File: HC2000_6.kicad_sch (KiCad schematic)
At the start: 31 parts, among them Q1 17,734, T2 2N2369/2N2368, T3 2N2369/BC108A

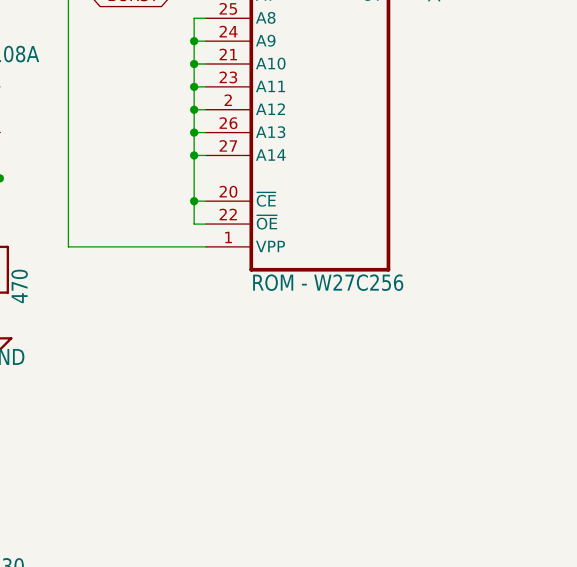
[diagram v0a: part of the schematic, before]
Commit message: Updated ICs values and positions
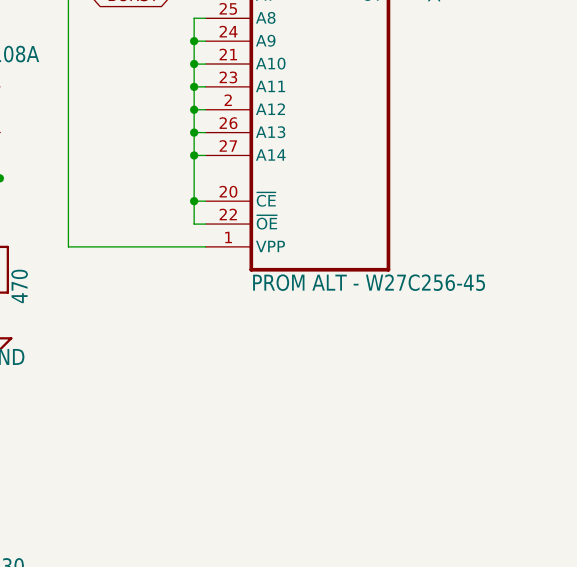
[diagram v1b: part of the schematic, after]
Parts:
- UB6: value ROM - W27C256 -> PROM ALT - W27C256-45
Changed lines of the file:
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@@
       (effects (font (size 1.778 1.5113)) (justify left bottom))
     )
-    (property "Value" "ROM - W27C256" (at 220.98 91.44 0)
+    (property "Value" "PROM ALT - W27C256-45" (at 220.98 91.44 0)
       (effects (font (size 1.778 1.5113)) (justify left bottom))
     )

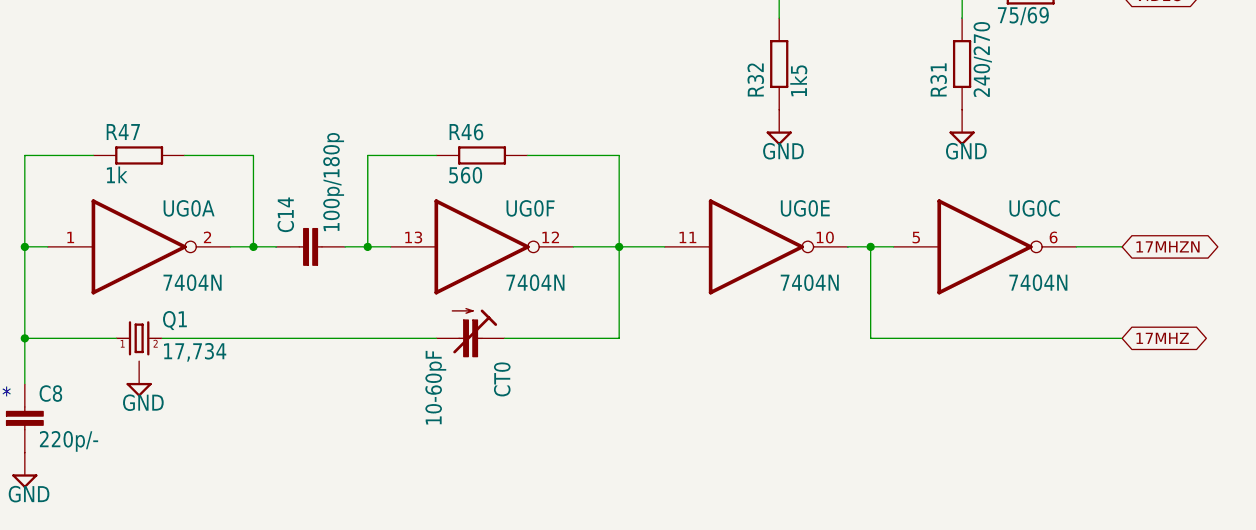
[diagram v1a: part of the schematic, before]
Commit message: Fix errors (IC & unnoticed cut for 1 EPROM)
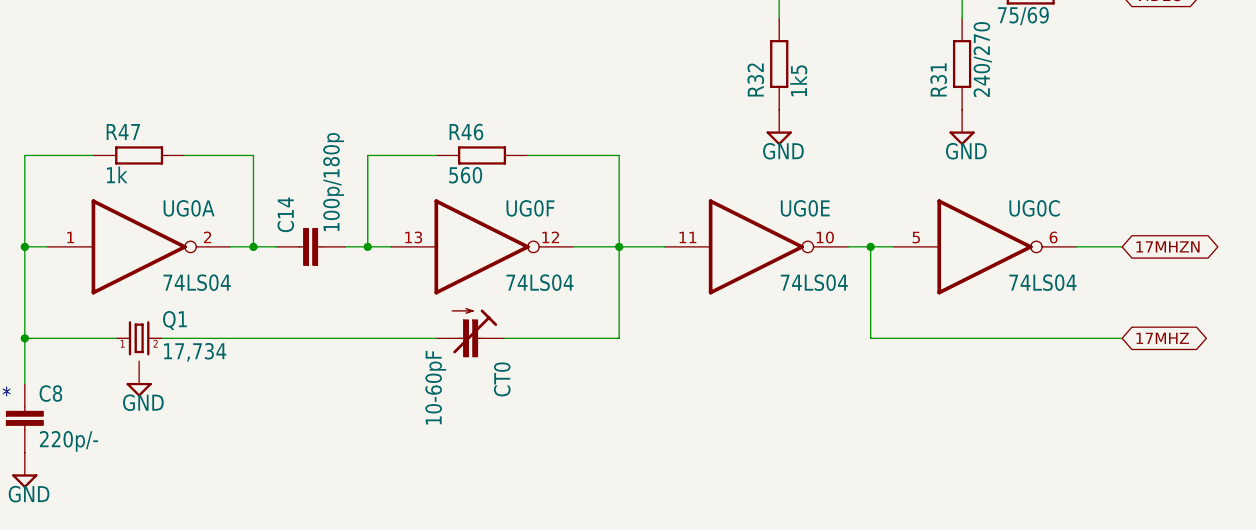
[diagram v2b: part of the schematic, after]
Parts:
- UG0: value 7404N -> 74LS04
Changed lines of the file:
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@@
       (effects (font (size 1.778 1.5113)) (justify left bottom))
     )
-    (property "Value" "7404N" (at 193.04 157.48 0)
+    (property "Value" "74LS04" (at 193.04 157.48 0)
       (effects (font (size 1.778 1.5113)) (justify left bottom))
     )
@@
       (effects (font (size 1.778 1.5113)) (justify left bottom))
     )
-    (property "Value" "7404N" (at 167.64 157.48 0)
+    (property "Value" "74LS04" (at 167.64 157.48 0)
       (effects (font (size 1.778 1.5113)) (justify left bottom))
     )
@@
       (effects (font (size 1.778 1.5113)) (justify left bottom))
     )
-    (property "Value" "7404N" (at 137.16 157.48 0)
+    (property "Value" "74LS04" (at 137.16 157.48 0)
       (effects (font (size 1.778 1.5113)) (justify left bottom))
     )
@@
       (effects (font (size 1.778 1.5113)) (justify left bottom))
     )
-    (property "Value" "7404N" (at 99.06 157.48 0)
-      (effects (font (size 1.778 1.5113)) (justify left bottom))
-    )
+    (property "Value" "74LS04" (at 99.06 157.48 0)
+      (effects (font (size 1.778 1.5113)) (justify left bottom))
+    )

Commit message: Revision-E
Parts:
- C14: value 100p/180p -> 180p
- C7: value 10p/15p -> 15p
- C8: value 220p/- -> -
- R30, R48: value 75/69 -> 69
- R31: value 240/270 -> 270
- R66: value 1k8/1k6 -> 1k6
- R68: value 5k6/5k1 -> 5k1
- T2: value 2N2369/2N2368 -> 2N2368
- T3: value 2N2369/BC108A -> BC108A
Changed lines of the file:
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@@
       (effects (font (size 1.778 1.5113)) (justify left bottom))
     )
-    (property "Value" "240/270" (at 191.262 135.89 0)
+    (property "Value" "270" (at 191.262 135.89 0)
       (effects (font (size 1.778 1.5113)) (justify left bottom))
     )
@@
       (effects (font (size 1.778 1.5113)) (justify left bottom))
     )
-    (property "Value" "100p/180p" (at 118.999 150.876 0)
+    (property "Value" "180p" (at 118.999 150.876 0)
       (effects (font (size 1.778 1.5113)) (justify left bottom))
     )
@@
       (effects (font (size 1.778 1.5113)) (justify left bottom))
     )
-    (property "Value" "2N2369/2N2368" (at 175.26 111.76 0)
+    (property "Value" "2N2368" (at 175.26 111.76 0)
       (effects (font (size 1.778 1.5113)) (justify left bottom))
     )
@@
       (effects (font (size 1.778 1.5113)) (justify left bottom))
     )
-    (property "Value" "75/69" (at 170.942 67.31 0)
+    (property "Value" "69" (at 170.942 67.31 0)
       (effects (font (size 1.778 1.5113)) (justify left bottom))
     )
@@
       (effects (font (size 1.778 1.5113)) (justify left bottom))
     )
-    (property "Value" "75/69" (at 191.77 127.762 0)
+    (property "Value" "69" (at 191.77 127.762 0)
       (effects (font (size 1.778 1.5113)) (justify left bottom))
     )
@@
       (effects (font (size 1.778 1.5113)) (justify left bottom))
     )
-    (property "Value" "2N2369/BC108A" (at 180.34 66.04 0)
+    (property "Value" "BC108A" (at 180.34 66.04 0)
       (effects (font (size 1.778 1.5113)) (justify left bottom))
     )
@@
       (effects (font (size 1.778 1.5113)) (justify left bottom))
     )
-    (property "Value" "5k6/5k1" (at 140.97 104.902 0)
+    (property "Value" "5k1" (at 140.97 104.902 0)
       (effects (font (size 1.778 1.5113)) (justify left bottom))
     )
@@
       (effects (font (size 1.778 1.5113)) (justify left bottom))
     )
-    (property "Value" "1k8/1k6" (at 140.97 120.142 0)
+    (property "Value" "1k6" (at 140.97 120.142 0)
       (effects (font (size 1.778 1.5113)) (justify left bottom))
     )
@@
       (effects (font (size 1.778 1.5113)) (justify left bottom))
     )
-    (property "Value" "220p/-" (at 85.344 174.879 0)
+    (property "Value" "-" (at 85.344 174.879 0)
       (effects (font (size 1.778 1.5113)) (justify left bottom))
     )
@@
       (effects (font (size 1.778 1.5113)) (justify left bottom))
     )
-    (property "Value" "10p/15p" (at 169.164 108.839 0)
-      (effects (font (size 1.778 1.5113)) (justify left bottom))
-    )
+    (property "Value" "15p" (at 169.164 108.839 0)
+      (effects (font (size 1.778 1.5113)) (justify left bottom))
+    )

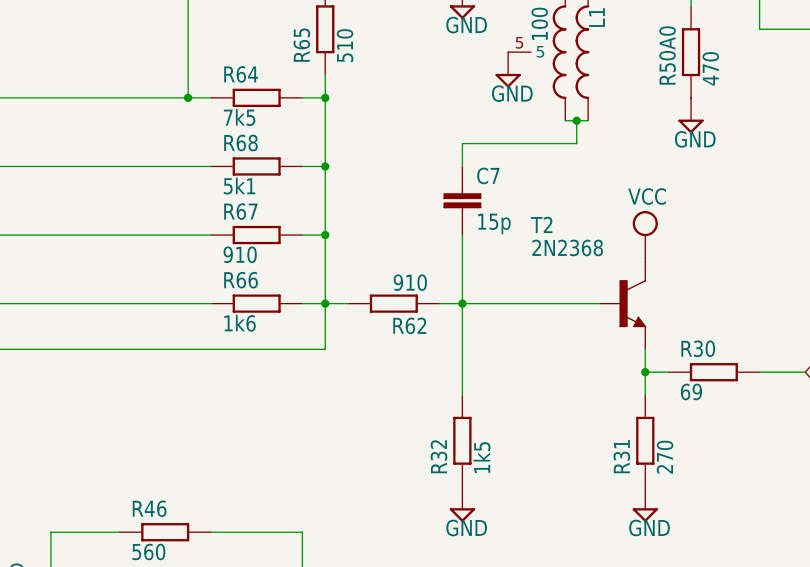
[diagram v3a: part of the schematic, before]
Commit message: A few minor changes
R62 has value 470 instead of 910 and C6 is missing.
Connected a few conector's shield pins to GND.
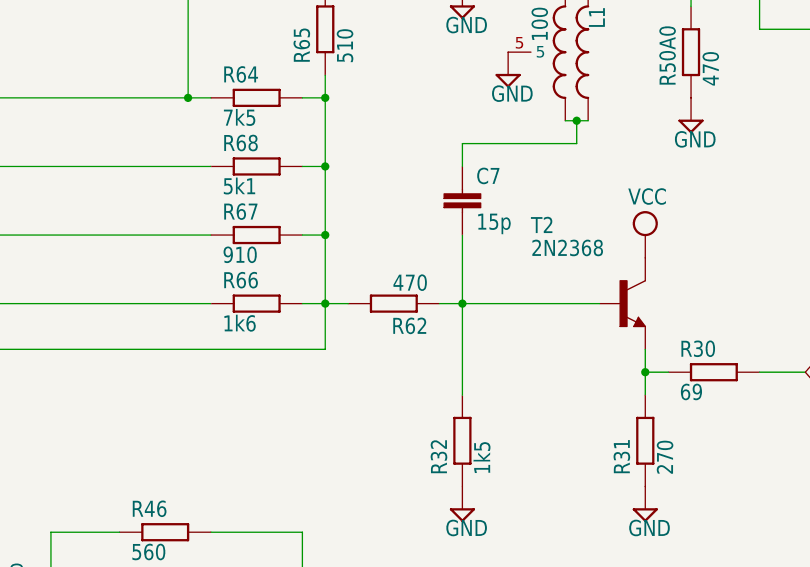
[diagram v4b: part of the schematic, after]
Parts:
- R62: value 910 -> 470
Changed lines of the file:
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@@
       (effects (font (size 1.778 1.5113)) (justify left bottom))
     )
-    (property "Value" "910" (at 163.83 113.538 0)
+    (property "Value" "470" (at 163.83 113.538 0)
       (effects (font (size 1.778 1.5113)) (justify left bottom))
     )

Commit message: Revision E final fixes before fork
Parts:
- L1: value 100 -> 100mH
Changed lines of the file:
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@@
       (effects (font (size 1.778 1.5113)) (justify left bottom))
     )
-    (property "Value" "100" (at 175.26 83.82 90)
+    (property "Value" "100mH" (at 175.26 83.82 90)
       (effects (font (size 1.778 1.5113)) (justify left bottom))
     )
